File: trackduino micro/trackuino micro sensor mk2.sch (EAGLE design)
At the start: 43 parts, among them IC2 74AHC1G125DBV, SW1 SPST_TACT-KMR2, U1 ATMEGA168MLF, U2 SHT21, Y1 16MHZ

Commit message: sht21 routing
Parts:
- renumbered LED3 to VCC, LED4 to PTT, U2 to SHT21
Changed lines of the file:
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@@
 <part name="SUPPLY4" library="SparkFun-Aesthetics" deviceset="VCC" device=""/>
 <part name="SUPPLY5" library="SparkFun-Aesthetics" deviceset="VCC" device=""/>
-<part name="LED3" library="adafruit" deviceset="LED" device="CHIP-LED0805"/>
+<part name="VCC" library="adafruit" deviceset="LED" device="CHIP-LED0805"/>
 <part name="R4" library="SparkFun-Resistors" deviceset="RESISTOR" device="0805-RES" value="330ohm"/>
 <part name="GND19" library="SparkFun-Aesthetics" deviceset="GND" device=""/>
@@
 <part name="SUPPLY11" library="SparkFun-Aesthetics" deviceset="VCC" device=""/>
 <part name="GND25" library="SparkFun-Aesthetics" deviceset="GND" device=""/>
-<part name="LED4" library="adafruit" deviceset="LED" device="CHIP-LED0805"/>
+<part name="PTT" library="adafruit" deviceset="LED" device="CHIP-LED0805"/>
 <part name="R6" library="SparkFun-Resistors" deviceset="RESISTOR" device="0805-RES" value="330ohm"/>
 <part name="GND26" library="SparkFun-Aesthetics" deviceset="GND" device=""/>
@@
 <part name="C9" library="resistor" deviceset="C-US" device="C1206" value="100uf"/>
 <part name="GND31" library="SparkFun-Aesthetics" deviceset="GND" device=""/>
-<part name="U2" library="sht21" deviceset="SHT21" device=""/>
+<part name="SHT21" library="sht21" deviceset="SHT21" device=""/>
 </parts>
 <sheets>
@@
 <instance part="SUPPLY4" gate="G$1" x="55.88" y="160.02" rot="R90"/>
 <instance part="SUPPLY5" gate="G$1" x="55.88" y="152.4" rot="R90"/>
-<instance part="LED3" gate="G$1" x="167.64" y="76.2" rot="R180"/>
+<instance part="VCC" gate="G$1" x="167.64" y="76.2" rot="R180"/>
 <instance part="R4" gate="G$1" x="167.64" y="68.58" rot="R270"/>
 <instance part="GND19" gate="1" x="167.64" y="83.82" rot="R180"/>
@@
 <instance part="SUPPLY11" gate="G$1" x="25.4" y="63.5" rot="R90"/>
 <instance part="GND25" gate="1" x="22.86" y="17.78" rot="R270"/>
-<instance part="LED4" gate="G$1" x="160.02" y="76.2" rot="R180"/>
+<instance part="PTT" gate="G$1" x="160.02" y="76.2" rot="R180"/>
 <instance part="R6" gate="G$1" x="160.02" y="68.58" rot="R270"/>
 <instance part="GND26" gate="1" x="160.02" y="83.82" rot="R180"/>
@@
 <instance part="C9" gate="G$1" x="58.42" y="137.16"/>
 <instance part="GND31" gate="1" x="58.42" y="129.54"/>
-<instance part="U2" gate="A" x="121.92" y="83.82"/>
+<instance part="SHT21" gate="A" x="121.92" y="83.82"/>
 </instances>
 <busses>
@@
 </segment>
 <segment>
-<pinref part="LED3" gate="G$1" pin="C"/>
+<pinref part="VCC" gate="G$1" pin="C"/>
 <pinref part="GND19" gate="1" pin="GND"/>
 <junction x="167.64" y="81.28"/>
@@
 </segment>
 <segment>
-<pinref part="LED4" gate="G$1" pin="C"/>
+<pinref part="PTT" gate="G$1" pin="C"/>
 <pinref part="GND26" gate="1" pin="GND"/>
 <junction x="160.02" y="81.28"/>
@@
 </segment>
 <segment>
-<pinref part="U2" gate="A" pin="VSS"/>
+<pinref part="SHT21" gate="A" pin="VSS"/>
 <pinref part="GND20" gate="1" pin="GND"/>
 <junction x="104.14" y="73.66"/>
@@
 <wire x1="104.14" y1="91.44" x2="101.6" y2="91.44" width="0.1524" layer="91"/>
 <label x="101.6" y="91.44" size="1.778" layer="95"/>
-<pinref part="U2" gate="A" pin="VDD"/>
+<pinref part="SHT21" gate="A" pin="VDD"/>
 <junction x="104.14" y="91.44"/>
 </segment>
@@
 <net name="N$8" class="0">
 <segment>
-<pinref part="LED3" gate="G$1" pin="A"/>
+<pinref part="VCC" gate="G$1" pin="A"/>
 <pinref part="R4" gate="G$1" pin="1"/>
 <junction x="167.64" y="73.66"/>
@@
 <net name="N$27" class="0">
 <segment>
-<pinref part="LED4" gate="G$1" pin="A"/>
+<pinref part="PTT" gate="G$1" pin="A"/>
 <pinref part="R6" gate="G$1" pin="1"/>
 <junction x="160.02" y="73.66"/>
@@
 <wire x1="142.24" y1="91.44" x2="139.7" y2="91.44" width="0.1524" layer="91"/>
 <label x="139.7" y="91.44" size="1.778" layer="95"/>
-<pinref part="U2" gate="A" pin="SDA"/>
+<pinref part="SHT21" gate="A" pin="SDA"/>
 <junction x="139.7" y="91.44"/>
 </segment>
@@
 <wire x1="104.14" y1="86.36" x2="101.6" y2="86.36" width="0.1524" layer="91"/>
 <label x="101.6" y="86.36" size="1.778" layer="95"/>
-<pinref part="U2" gate="A" pin="SCL"/>
+<pinref part="SHT21" gate="A" pin="SCL"/>
 <junction x="104.14" y="86.36"/>
 </segment>

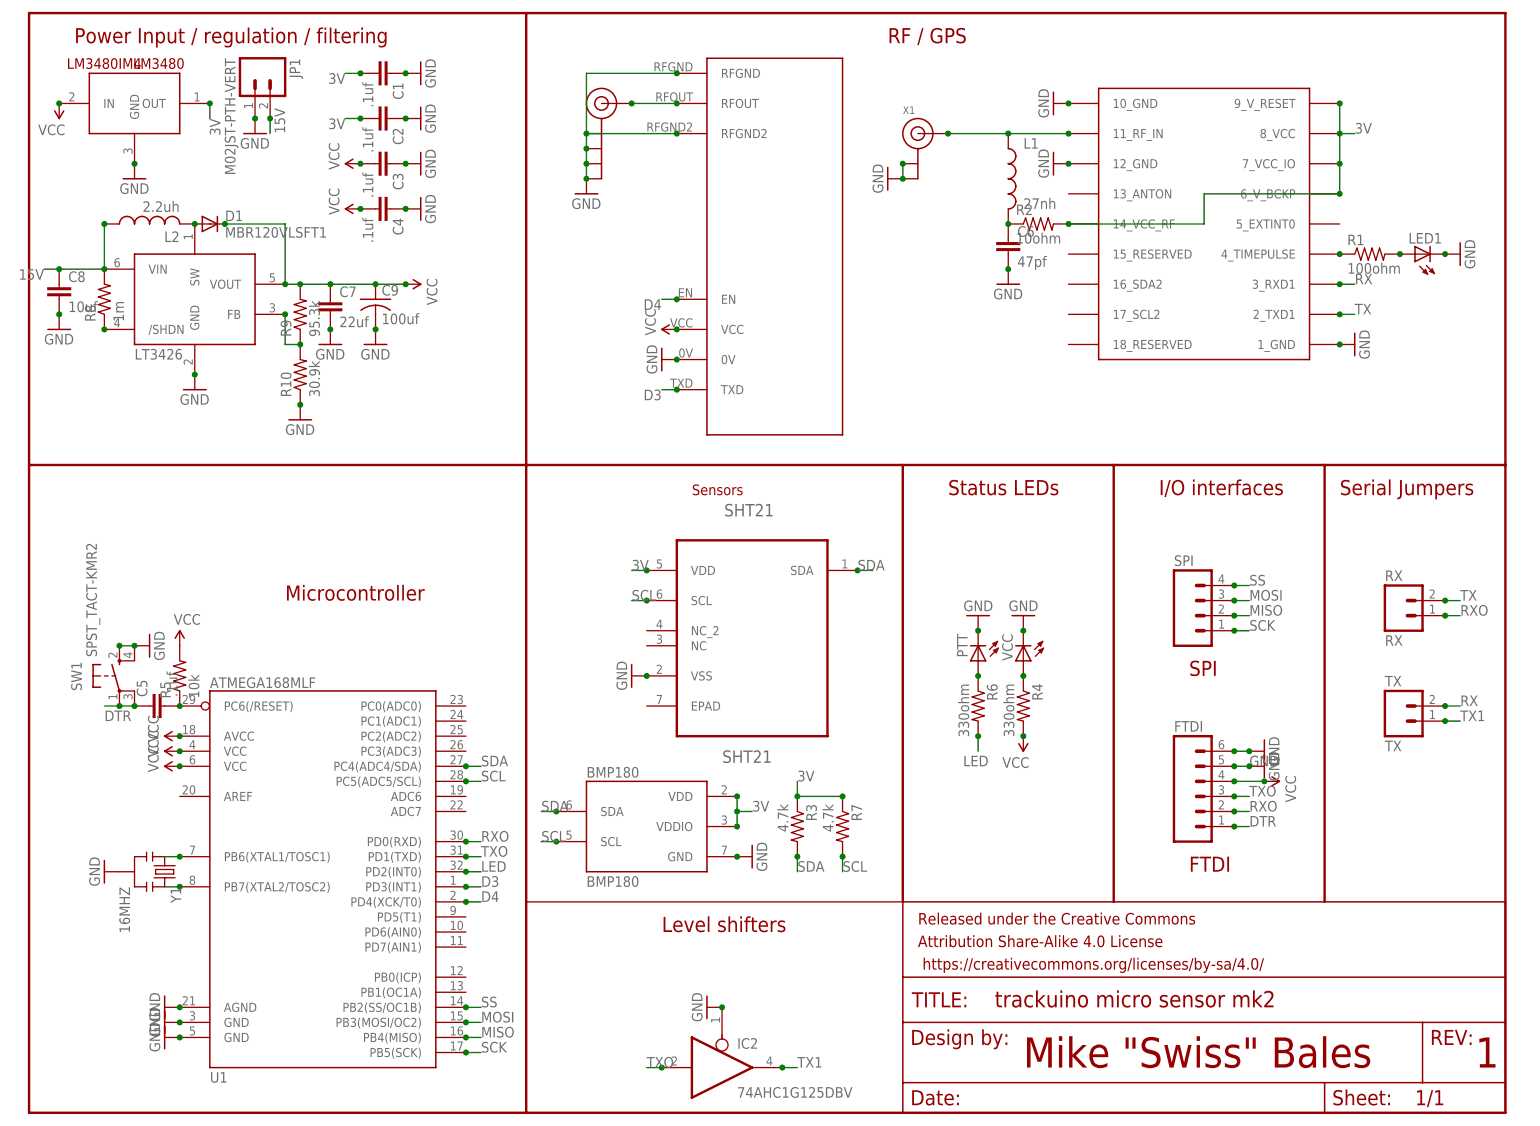
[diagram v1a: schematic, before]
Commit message: added i2c breakout and fixed ftdi
added breakouts on all versions for i2c next to the spi header, replaced
IO breakout headers from .1" to 2mm to accomodate i2c.
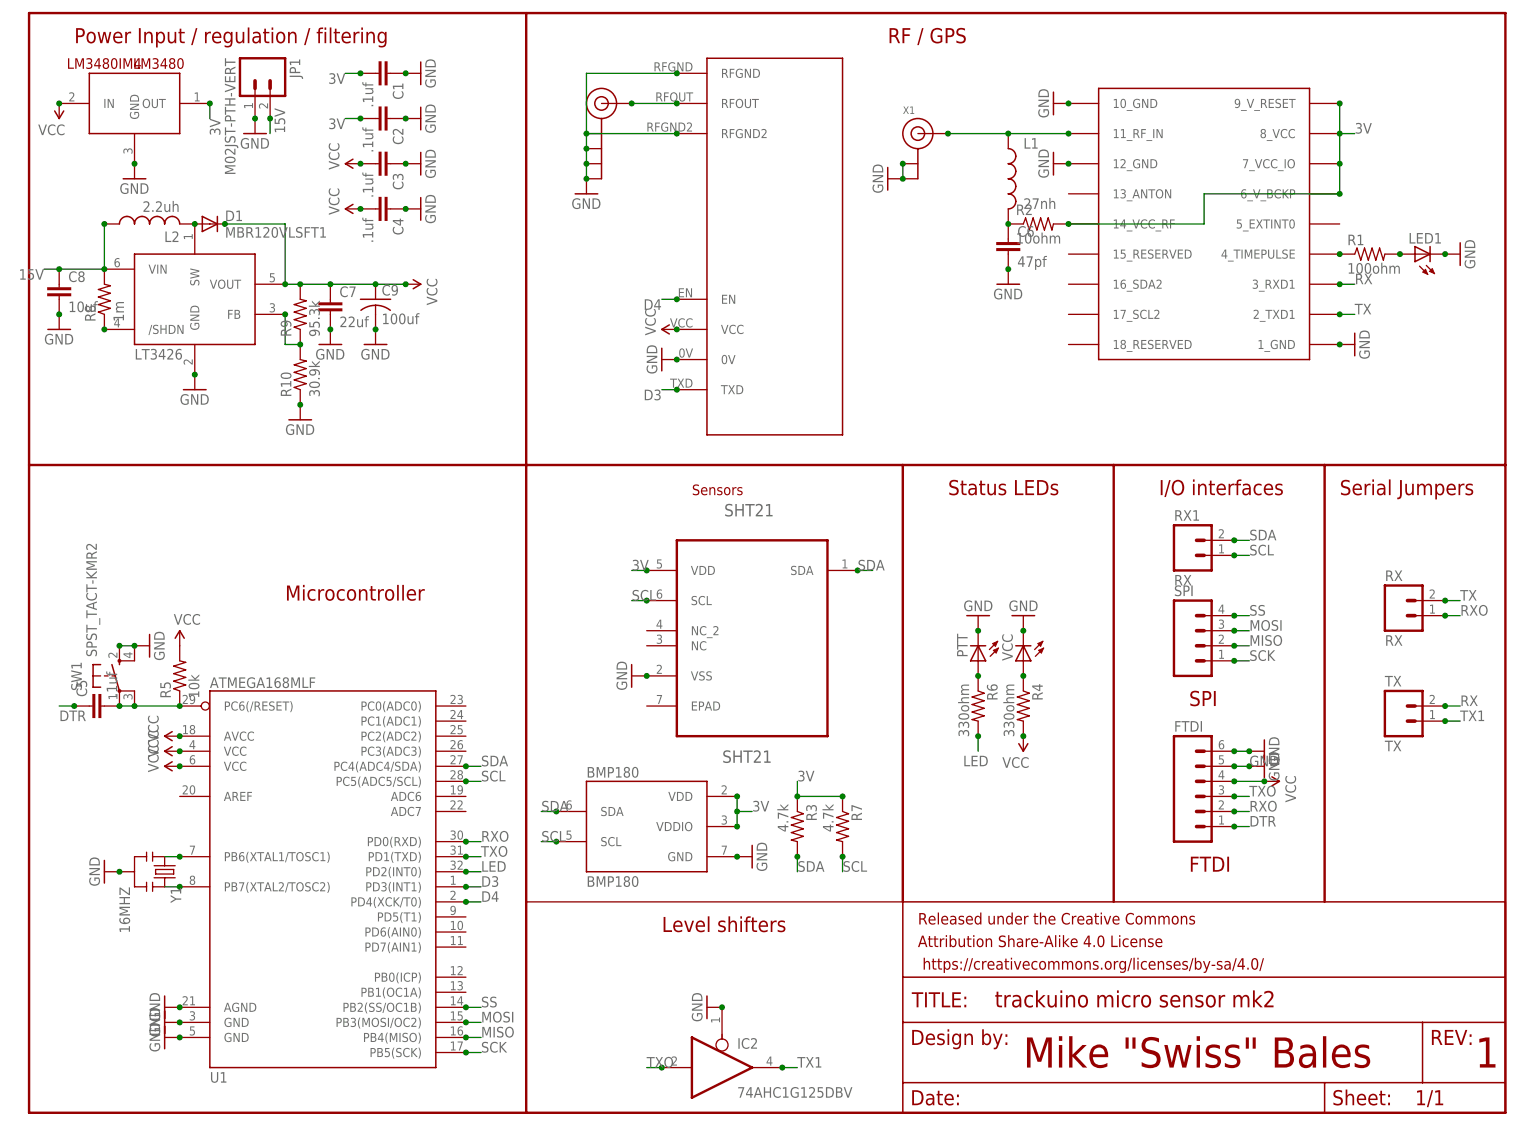
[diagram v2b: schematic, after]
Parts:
- added RX1: RX, SparkFun-Connectors:M02JST-PTH-VERT
- SPI: device SparkFun-Connectors:M041X04_NO_SILK -> SparkFun-Connectors:M04JST-PTH-VERT
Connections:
- removed net N$7: C5.2, R5.1, U1.PC6(/RESET)
- new net N$17: C5.2, R5.1, SW1.P, SW1.P1, U1.PC6(/RESET)
- net DTR: no longer SW1.P, SW1.P1
- net SCL: now also RX1.1
- net SDA: now also RX1.2
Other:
- moved on the sheet: C5, SPI
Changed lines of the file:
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@@
 <part name="C5" library="SparkFun-Capacitors" deviceset="CAP" device="0805" value=".1uf"/>
 <part name="TX" library="SparkFun-Connectors" deviceset="M02" device="PTH" value="TX"/>
-<part name="SPI" library="SparkFun-Connectors" deviceset="M04" device="1X04_NO_SILK"/>
+<part name="SPI" library="SparkFun-Connectors" deviceset="M04" device="JST-PTH-VERT"/>
 <part name="GND23" library="SparkFun-Aesthetics" deviceset="GND" device=""/>
 <part name="FRAME1" library="SparkFun-Aesthetics" deviceset="FRAME-LETTER" device=""/>
@@
 <part name="GND31" library="SparkFun-Aesthetics" deviceset="GND" device=""/>
 <part name="SHT21" library="sht21" deviceset="SHT21" device=""/>
+<part name="RX1" library="SparkFun-Connectors" deviceset="M02" device="JST-PTH-VERT" value="RX"/>
 </parts>
 <sheets>
@@
 <text x="190.5" y="104.14" size="2.54" layer="94">I/O interfaces</text>
 <text x="220.98" y="104.14" size="2.54" layer="94">Serial Jumpers</text>
-<text x="195.58" y="73.66" size="2.54" layer="94">SPI</text>
+<text x="195.58" y="68.58" size="2.54" layer="94">SPI</text>
 <text x="195.58" y="40.64" size="2.54" layer="94">FTDI</text>
 <wire x1="147.32" y1="35.56" x2="83.82" y2="35.56" width="0.1524" layer="94"/>
@@
 <instance part="R5" gate="G$1" x="25.4" y="73.66" rot="R90"/>
 <instance part="SUPPLY10" gate="G$1" x="25.4" y="78.74"/>
-<instance part="C5" gate="G$1" x="22.86" y="68.58" rot="R90"/>
+<instance part="C5" gate="G$1" x="12.7" y="68.58" rot="R90"/>
 <instance part="TX" gate="G$1" x="231.14" y="66.04"/>
-<instance part="SPI" gate="G$1" x="198.12" y="83.82"/>
+<instance part="SPI" gate="G$1" x="198.12" y="78.74"/>
 <instance part="GND23" gate="1" x="20.32" y="78.74" rot="R90"/>
 <instance part="FRAME1" gate="G$1" x="0" y="0"/>
@@
 <instance part="GND31" gate="1" x="58.42" y="129.54"/>
 <instance part="SHT21" gate="A" x="121.92" y="83.82"/>
+<instance part="RX1" gate="G$1" x="195.58" y="93.98"/>
 </instances>
 <busses>
@@
 <pinref part="GND24" gate="1" pin="GND"/>
 <pinref part="Y1" gate="G$1" pin="2"/>
+<junction x="15.24" y="40.64"/>
 </segment>
 <segment>
@@
 </segment>
 <segment>
-<pinref part="SW1" gate="G$1" pin="P"/>
-<wire x1="15.24" y1="68.58" x2="17.78" y2="68.58" width="0.1524" layer="91"/>
-<pinref part="SW1" gate="G$1" pin="P1"/>
 <pinref part="C5" gate="G$1" pin="1"/>
-<junction x="17.78" y="68.58"/>
-<junction x="15.24" y="68.58"/>
-<wire x1="15.24" y1="68.58" x2="12.7" y2="68.58" width="0.1524" layer="91"/>
-<label x="12.7" y="66.04" size="1.778" layer="95"/>
+<wire x1="7.62" y1="68.58" x2="5.08" y2="68.58" width="0.1524" layer="91"/>
+<junction x="7.62" y="68.58"/>
+<label x="5.08" y="66.04" size="1.778" layer="95"/>
 </segment>
 </net>
@@
 <segment>
 <pinref part="SPI" gate="G$1" pin="2"/>
-<wire x1="203.2" y1="83.82" x2="205.74" y2="83.82" width="0.1524" layer="91"/>
-<label x="205.74" y="83.82" size="1.778" layer="95"/>
-<junction x="203.2" y="83.82"/>
+<wire x1="203.2" y1="78.74" x2="205.74" y2="78.74" width="0.1524" layer="91"/>
+<label x="205.74" y="78.74" size="1.778" layer="95"/>
+<junction x="203.2" y="78.74"/>
 </segment>
 </net>
@@
 <segment>
 <pinref part="SPI" gate="G$1" pin="3"/>
-<wire x1="203.2" y1="86.36" x2="205.74" y2="86.36" width="0.1524" layer="91"/>
-<label x="205.74" y="86.36" size="1.778" layer="95"/>
-<junction x="203.2" y="86.36"/>
+<wire x1="203.2" y1="81.28" x2="205.74" y2="81.28" width="0.1524" layer="91"/>
+<label x="205.74" y="81.28" size="1.778" layer="95"/>
+<junction x="203.2" y="81.28"/>
 </segment>
 </net>
@@
 <segment>
 <pinref part="SPI" gate="G$1" pin="1"/>
-<wire x1="203.2" y1="81.28" x2="205.74" y2="81.28" width="0.1524" layer="91"/>
-<label x="205.74" y="81.28" size="1.778" layer="95"/>
-<junction x="203.2" y="81.28"/>
+<wire x1="203.2" y1="76.2" x2="205.74" y2="76.2" width="0.1524" layer="91"/>
+<label x="205.74" y="76.2" size="1.778" layer="95"/>
+<junction x="203.2" y="76.2"/>
 </segment>
 </net>
@@
 <segment>
 <pinref part="SPI" gate="G$1" pin="4"/>
-<wire x1="203.2" y1="88.9" x2="205.74" y2="88.9" width="0.1524" layer="91"/>
-<label x="205.74" y="88.9" size="1.778" layer="95"/>
-<junction x="203.2" y="88.9"/>
+<wire x1="203.2" y1="83.82" x2="205.74" y2="83.82" width="0.1524" layer="91"/>
+<label x="205.74" y="83.82" size="1.778" layer="95"/>
+<junction x="203.2" y="83.82"/>
 </segment>
 </net>
@@
 <junction x="129.54" y="43.18"/>
 </segment>
+<segment>
+<pinref part="RX1" gate="G$1" pin="2"/>
+<wire x1="203.2" y1="96.52" x2="205.74" y2="96.52" width="0.1524" layer="91"/>
+<junction x="203.2" y="96.52"/>
+<label x="205.74" y="96.52" size="1.778" layer="95"/>
+</segment>
 </net>
 <net name="SCL" class="0">
@@
 <label x="137.16" y="40.64" size="1.778" layer="95"/>
 <junction x="137.16" y="43.18"/>
+</segment>
+<segment>
+<pinref part="RX1" gate="G$1" pin="1"/>
+<wire x1="203.2" y1="93.98" x2="205.74" y2="93.98" width="0.1524" layer="91"/>
+<junction x="203.2" y="93.98"/>
+<label x="205.74" y="93.98" size="1.778" layer="95"/>
 </segment>
 </net>
@@
 </segment>
 </net>
-<net name="N$7" class="0">
-<segment>
-<pinref part="U1" gate="G$1" pin="PC6(/RESET)"/>
-<pinref part="R5" gate="G$1" pin="1"/>
-<pinref part="C5" gate="G$1" pin="2"/>
-<junction x="25.4" y="68.58"/>
-<pinref part="C5" gate="G$1" pin="2"/>
-</segment>
-</net>
 <net name="N$9" class="0">
 <segment>
@@
 </segment>
 </net>
+<net name="N$17" class="0">
+<segment>
+<pinref part="C5" gate="G$1" pin="2"/>
+<pinref part="C5" gate="G$1" pin="2"/>
+<pinref part="U1" gate="G$1" pin="PC6(/RESET)"/>
+<pinref part="R5" gate="G$1" pin="1"/>
+<wire x1="15.24" y1="68.58" x2="17.78" y2="68.58" width="0.1524" layer="91"/>
+<pinref part="SW1" gate="G$1" pin="P"/>
+<junction x="15.24" y="68.58"/>
+<pinref part="SW1" gate="G$1" pin="P1"/>
+<junction x="17.78" y="68.58"/>
+<wire x1="17.78" y1="68.58" x2="25.4" y2="68.58" width="0.1524" layer="91"/>
+<junction x="25.4" y="68.58"/>
+</segment>
+</net>
